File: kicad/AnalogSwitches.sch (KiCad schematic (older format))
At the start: 63 parts

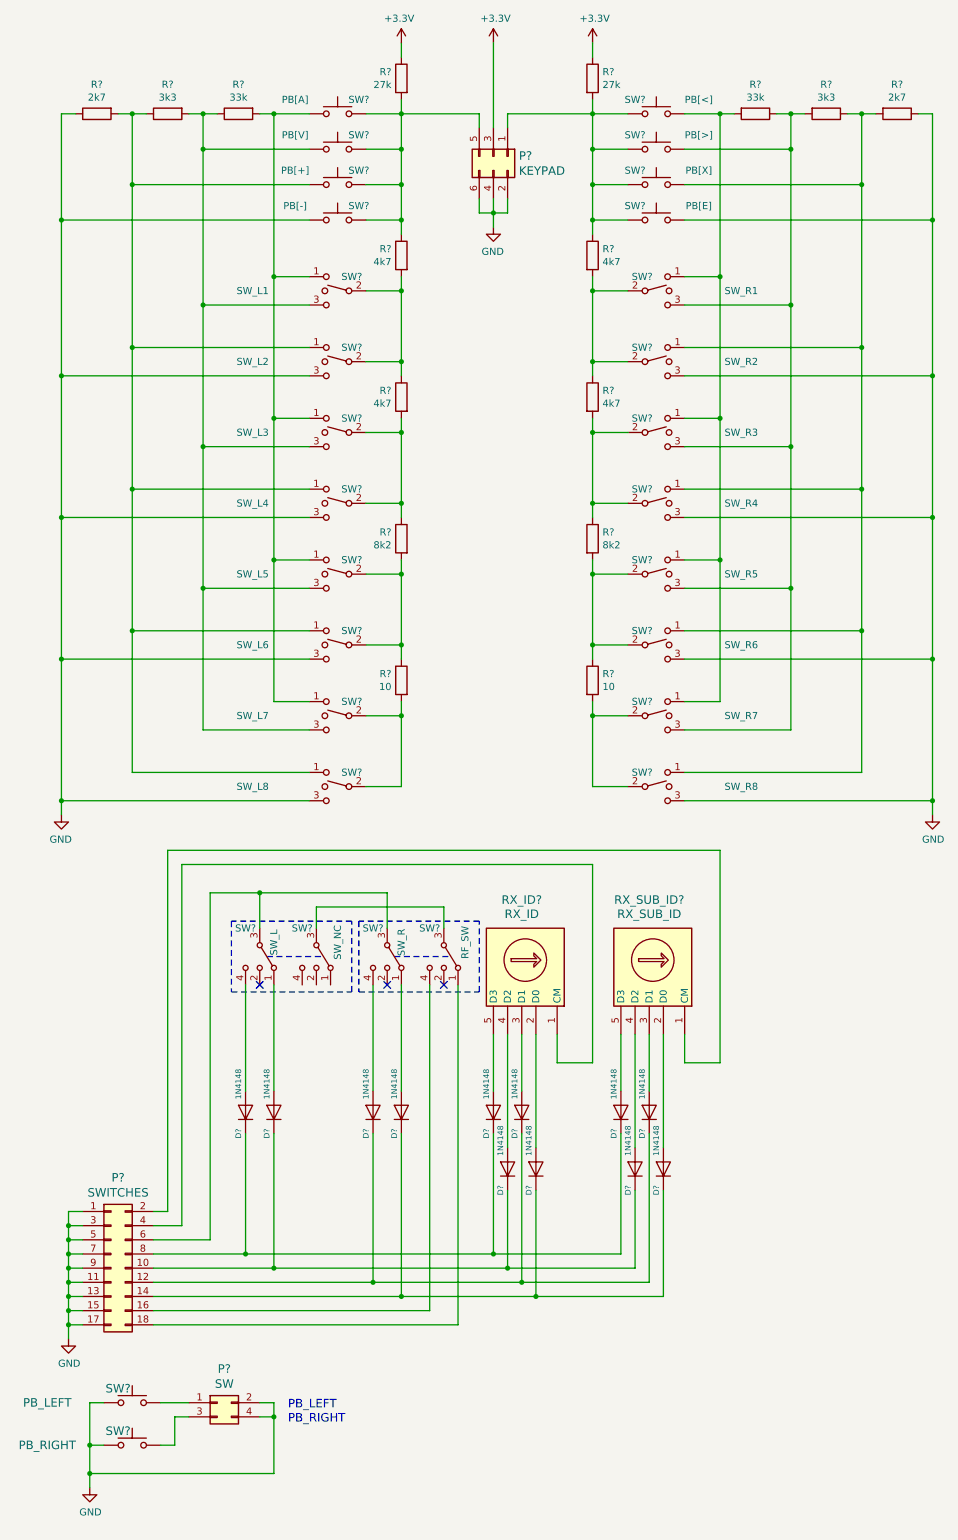
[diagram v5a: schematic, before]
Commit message: Replacing Si500/Si510 clock generator with i2c controlled Si514 model
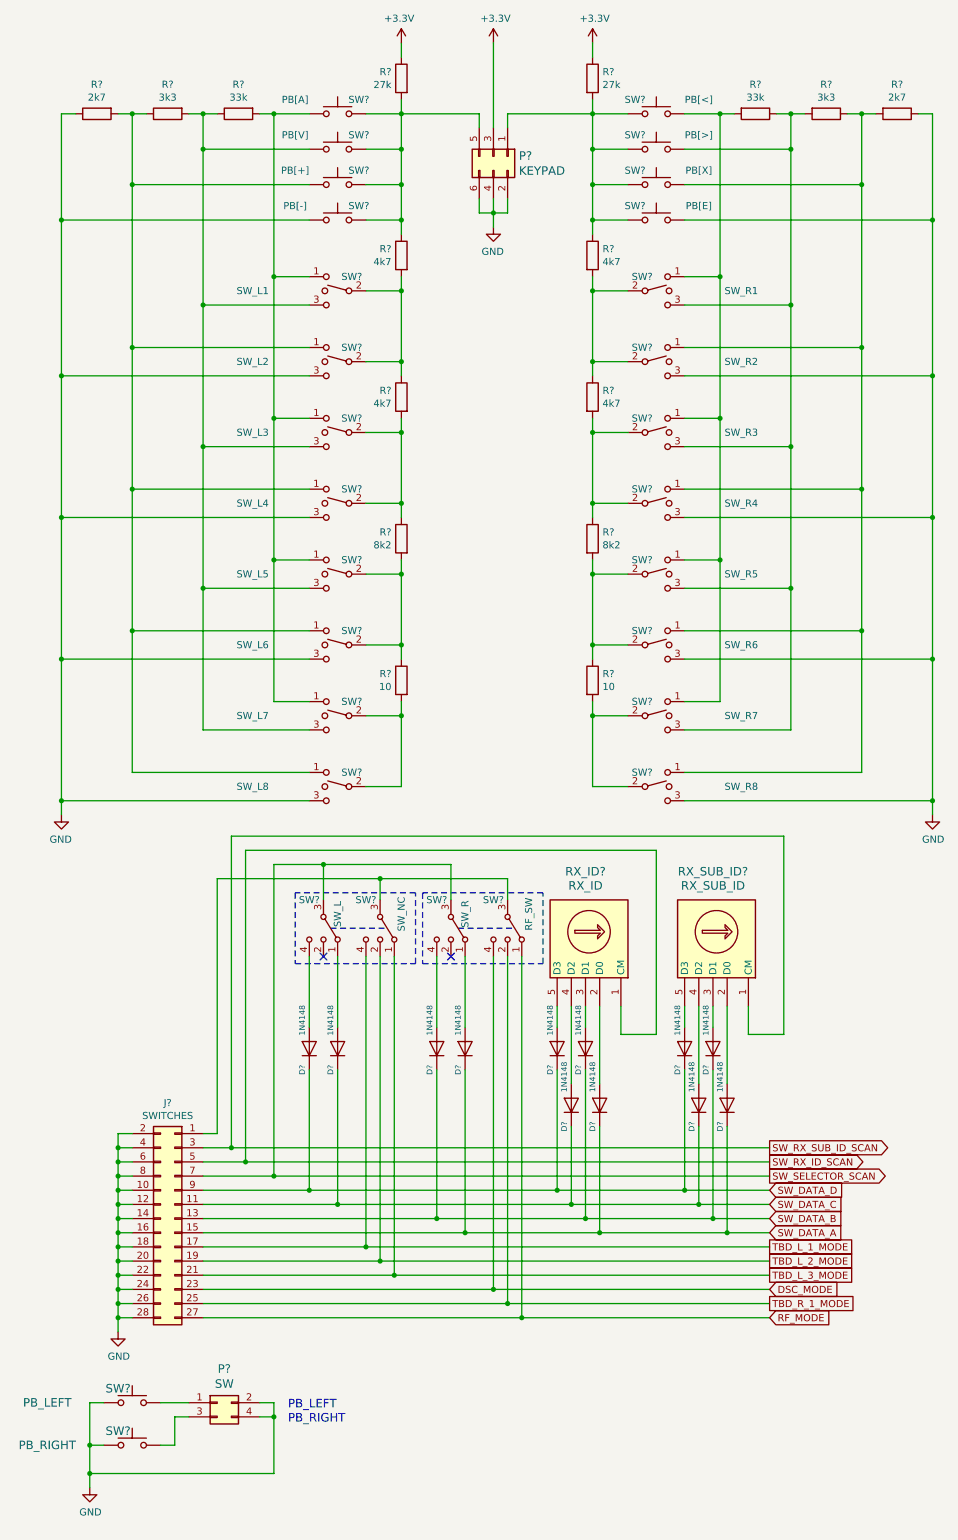
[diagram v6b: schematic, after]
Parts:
- removed P?: SWITCHES, symbol conn:Conn_02x09_Odd_Even
- added J?: SWITCHES, symbol conn:Conn_02x14_Odd_Even
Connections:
- net GND: now also J?.10 (Pin_10), J?.12 (Pin_12), J?.14 (Pin_14), J?.16 (Pin_16), J?.18 (Pin_18), J?.2 (Pin_2), J?.20 (Pin_20), J?.22 (Pin_22), J?.24 (Pin_24), J?.26 (Pin_26), J?.28 (Pin_28), J?.4 (Pin_4), J?.6 (Pin_6), J?.8 (Pin_8)
- net RF_MODE: now reaches SW?.1
- net RF_MODE: now also J?.27 (Pin_27)
- net TBD_R_1_MODE: now reaches SW?.2
- net TBD_R_1_MODE: now also J?.25 (Pin_25)
- net at SW?.3, SW?.3: now also J?.1 (Pin_1)
- net DSC_MODE: now reaches SW?.4
- net DSC_MODE: now also J?.23 (Pin_23)
- net SW_SELECTOR_SCAN: now reaches SW?.3, SW?.3
- net SW_SELECTOR_SCAN: now also J?.7 (Pin_7)
- net TBD_L_3_MODE: now reaches SW?.1
- net TBD_L_3_MODE: now also J?.21 (Pin_21)
- net TBD_L_2_MODE: now reaches SW?.2
- net TBD_L_2_MODE: now also J?.19 (Pin_19)
- net TBD_L_1_MODE: now reaches SW?.4
- net TBD_L_1_MODE: now also J?.17 (Pin_17)
- net SW_DATA_B: now reaches D?.1 (K), D?.1 (K), D?.1 (K)
- net SW_DATA_B: now also J?.13 (Pin_13)
- net SW_DATA_C: now reaches D?.1 (K), D?.1 (K), D?.1 (K)
- net SW_DATA_C: now also J?.11 (Pin_11)
- net SW_DATA_D: now reaches D?.1 (K), D?.1 (K), D?.1 (K)
- net SW_DATA_D: now also J?.9 (Pin_9)
- net SW_RX_SUB_ID_SCAN: now reaches HEX_SW?.1 (CM)
- net SW_RX_SUB_ID_SCAN: now also J?.3 (Pin_3)
- net SW_RX_ID_SCAN: now reaches HEX_SW?.1 (CM)
- net SW_RX_ID_SCAN: now also J?.5 (Pin_5)
- net SW_DATA_A: now reaches D?.1 (K), D?.1 (K), D?.1 (K)
- net SW_DATA_A: now also J?.15 (Pin_15)
- no-connect marks 3 -> 2
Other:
- moved on the sheet: D?, RX_ID?, RX_SUB_ID?, SW?
